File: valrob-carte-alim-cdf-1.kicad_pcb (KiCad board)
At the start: 4 copper layers, 87 x 57 mm, 201 parts, among them J1 USB_C_Receptacle_USB2.0_14P, J10 Conn_01x02, J11 Conn_01x02, J12 Conn_01x02, J13 Conn_01x02, J14 Conn_01x02, J15 Conn_01x02, J16 Conn_01x02, J17 Conn_01x02, J18 Conn_01x02, J19 Conn_01x02, J2 Conn_01x02, J20 Conn_01x02, J21 Conn_01x02, J22 Conn_01x02, J3 Conn_01x04_Pin, J4 Conn_01x02, J5 Conn_01x02, J6 Conn_01x02, J7 Conn_01x02, J8 Conn_01x02, J9 Conn_01x02, SW1 SW_Push, SW2 SW_Push, SW3 SW_Push, U1 SN65HVD230, U10 TPS259472A, U11 TPS259472A, U12 TPS259472A, U2 ESP32-S3-WROOM-1, U3 TLV75733PDBV, U4 TPS56A37, U5 TPS56A37, U6 TPS259472A, U7 TPS259472A, U8 TPS259472A, U9 TPS259472A

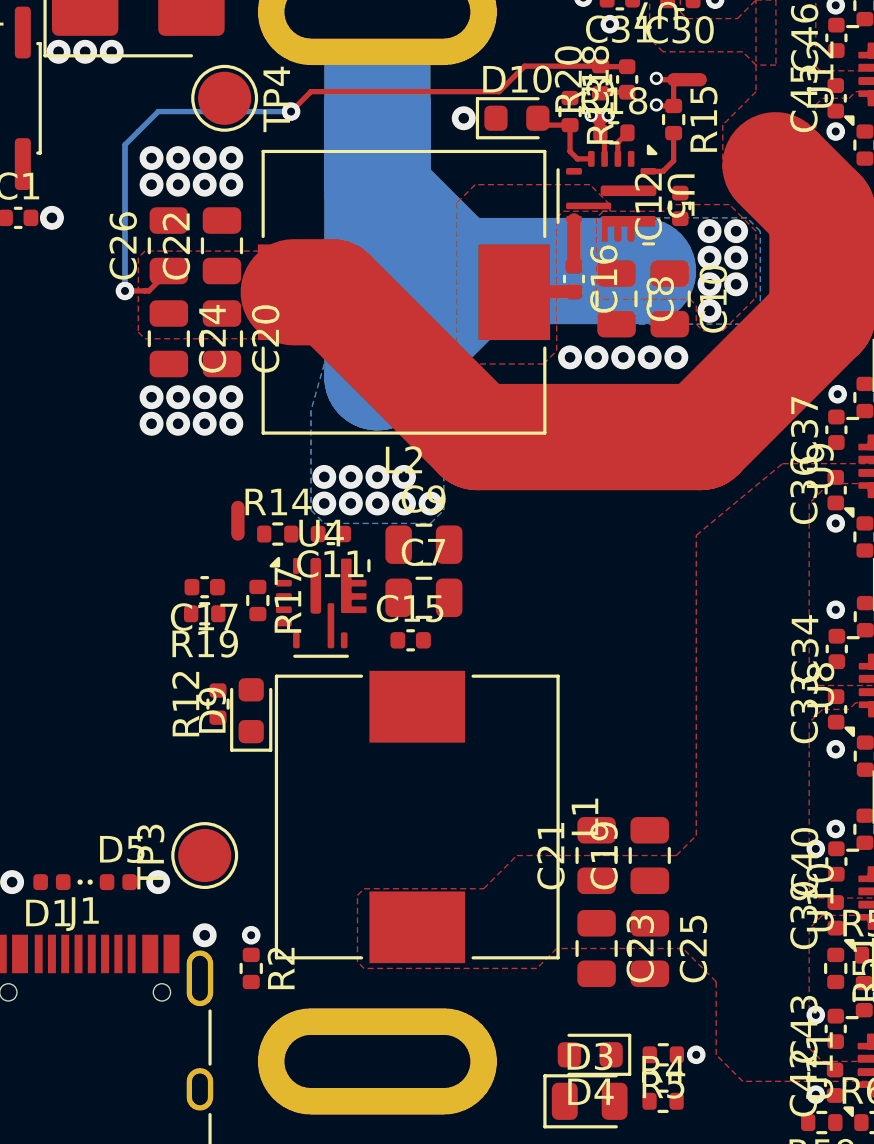
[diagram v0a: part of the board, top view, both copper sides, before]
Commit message: pcb: add 12V SMPS routing
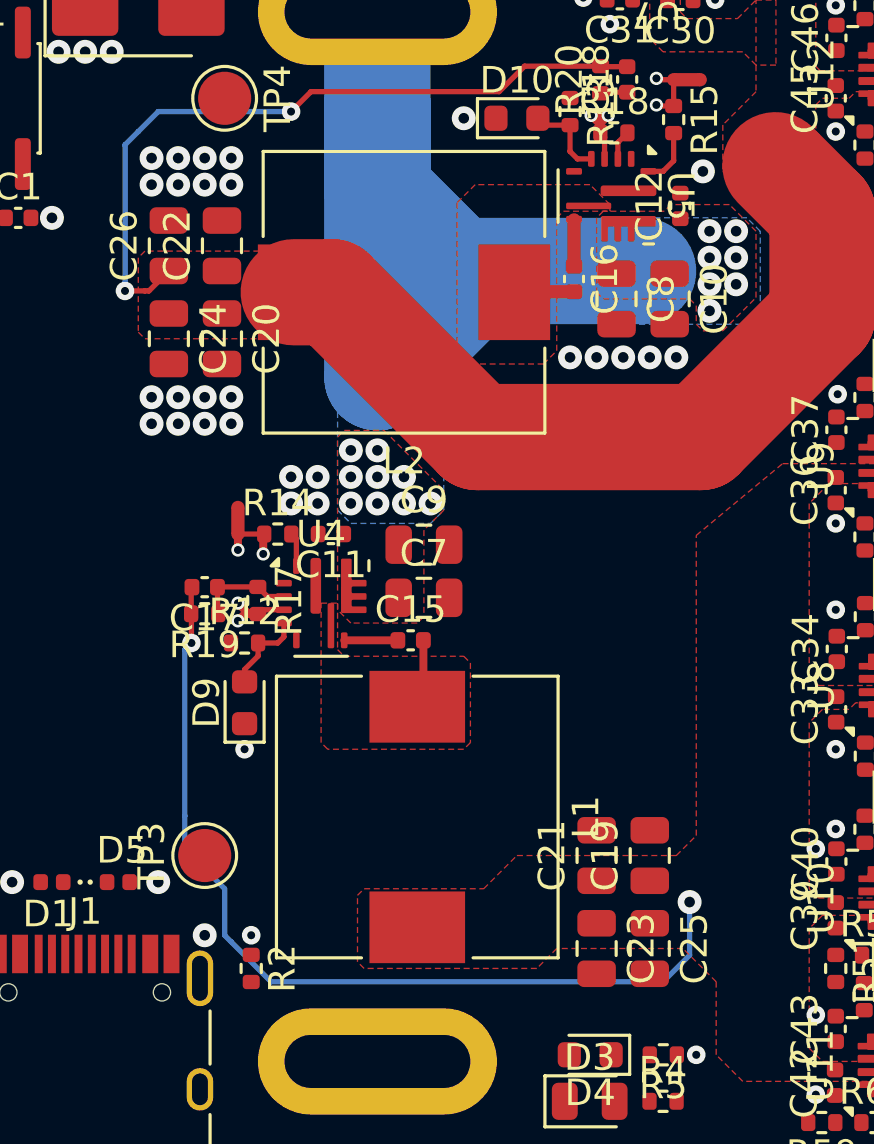
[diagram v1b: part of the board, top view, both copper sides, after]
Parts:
- moved R12 2.51 mm to (120.5, 90.2), turned to 0 degrees
- moved D9 0.39 mm to (120.5, 92.5)
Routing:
- net +12V: track 0.00 -> 34.5 mm, vias 0 -> 2
- net AGND: track 0.00 -> 5.18 mm, vias 0 -> 4
- net Net-(U4-FB): track 0.00 -> 3.67 mm
- net /PG_12V: track 0.00 -> 3.26 mm
- net Net-(U4-SW): track 0.00 -> 2.60 mm
- net Net-(U4-BOOT): track 0.00 -> 2.02 mm
- net Net-(U4-MODE): track 0.00 -> 1.28 mm
- net GND: vias 103 -> 109
- added copper zone on In1.Cu, net AGND
- added copper zone on F.Cu, net Net-(U4-SW)

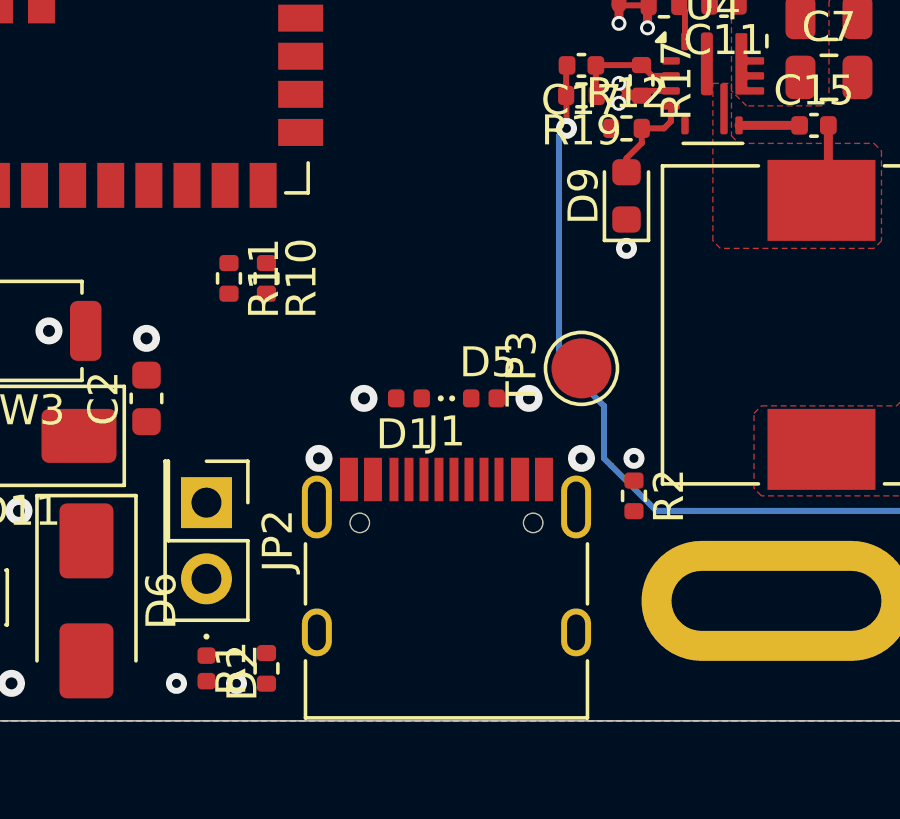
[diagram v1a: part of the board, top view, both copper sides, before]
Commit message: pcb: add usb routing
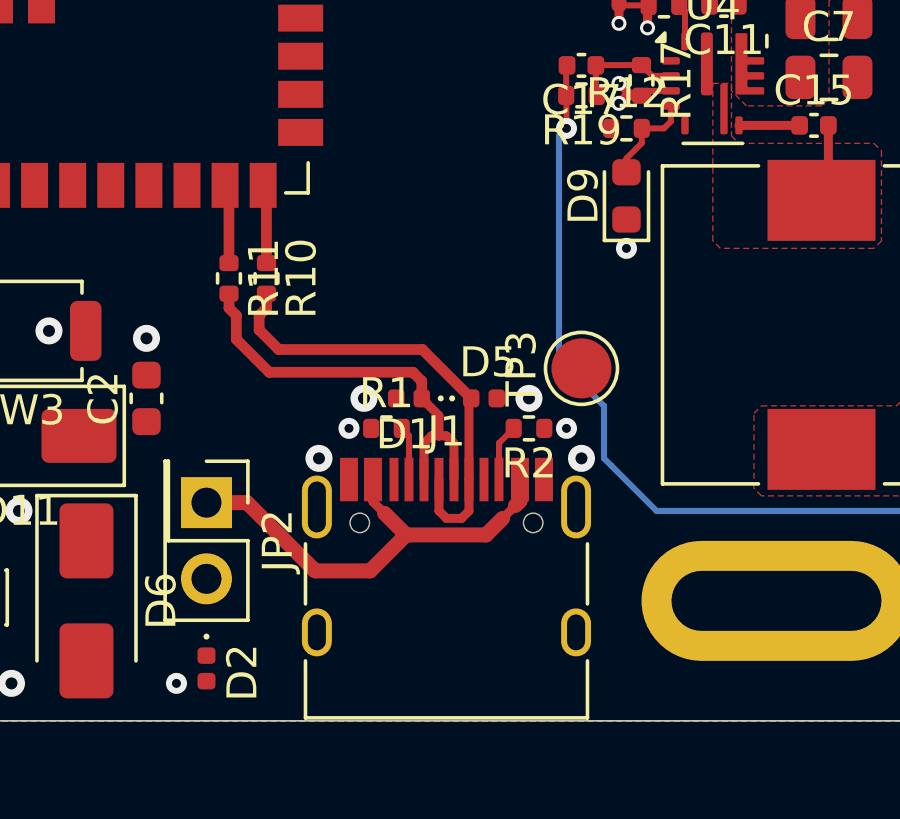
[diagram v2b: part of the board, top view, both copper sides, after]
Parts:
- moved R1 8.94 mm to (112.5, 100.2), turned to 0 degrees
- moved R2 4.16 mm to (117.2, 100.2), turned to 180 degrees
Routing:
- net VBUS: track 0.00 -> 15.4 mm
- net /D+: track 0.00 -> 15.4 mm
- net /D-: track 0.00 -> 14.1 mm
- net /ESP_D-: track 0.00 -> 2.64 mm
- net /ESP_D+: track 0.00 -> 2.64 mm
- net Net-(J1-CC2): track 0.00 -> 1.91 mm
- net Net-(J1-CC1): track 0.00 -> 1.80 mm

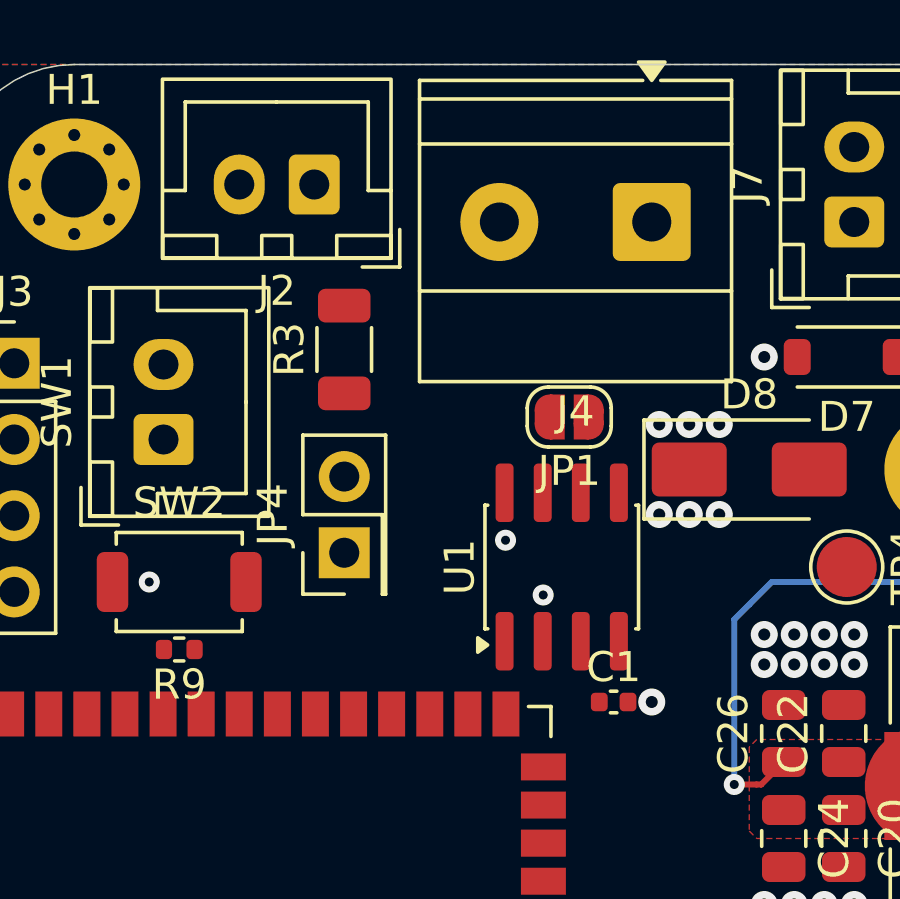
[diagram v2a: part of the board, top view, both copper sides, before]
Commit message: pcb: add can routing
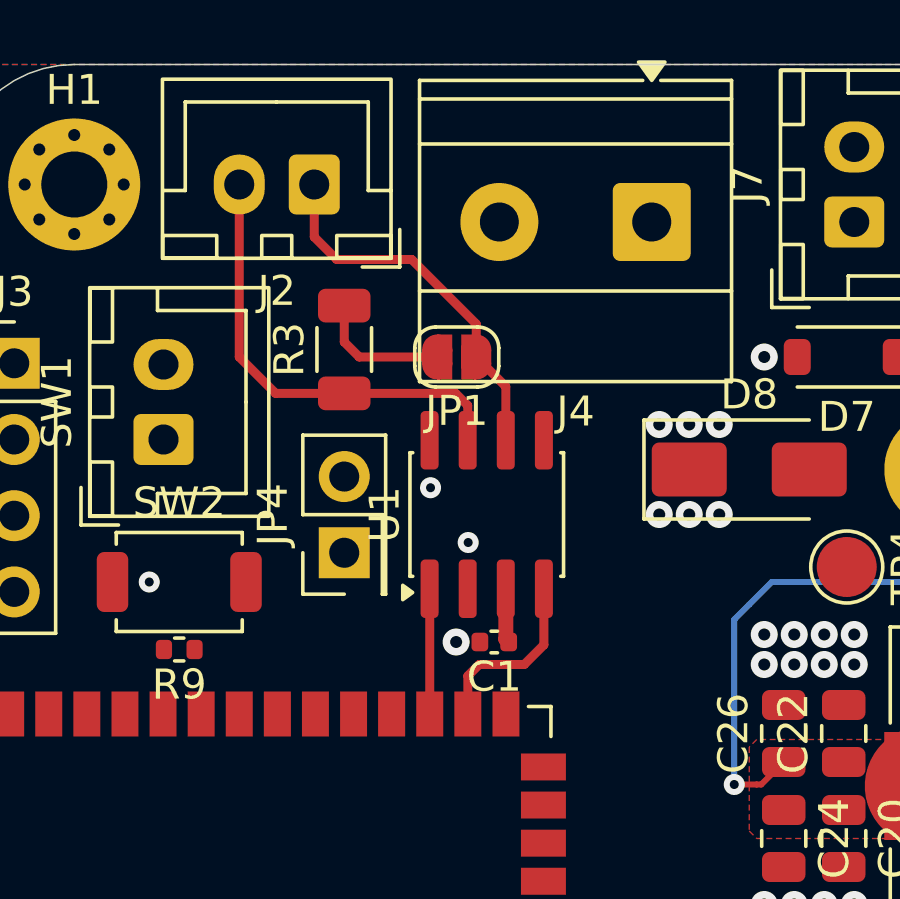
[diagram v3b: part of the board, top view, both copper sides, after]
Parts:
- moved C1 4.45 mm to (108.0, 72.2), turned to 180 degrees
- moved JP1 4.25 mm to (106.8, 62.8)
- moved U1 3.05 mm to (107.8, 68.0)
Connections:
- U2 pad 28: /BAU -> /CAN_RX
- U2 pad 29: /CAN_RX -> /CAN_TX
- U2 pad 30: /CAN_TX -> /BAU
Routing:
- net /CANH: track 0.00 -> 15.2 mm
- net /CANL: track 0.00 -> 12.6 mm
- net /CAN_RX: track 0.00 -> 6.10 mm
- net Net-(JP1-B): track 0.00 -> 4.52 mm
- net /CAN_TX: track 0.00 -> 4.18 mm
- net +3V3: track 0.00 -> 1.81 mm
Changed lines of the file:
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@@
 			(size 1.5 0.9)
 			(layers "F.Cu" "F.Mask" "F.Paste")
-			(net 89 "/BAU")
+			(net 91 "/CAN_RX")
 			(pinfunction "SPIIO6/GPIO35/FSPID/SUBSPID")
 			(pintype "bidirectional")
@@
 			(size 1.5 0.9)
 			(layers "F.Cu" "F.Mask" "F.Paste")
-			(net 91 "/CAN_RX")
+			(net 90 "/CAN_TX")
 			(pinfunction "SPIIO7/GPIO36/FSPICLK/SUBSPICLK")
 			(pintype "bidirectional")
@@
 			(size 1.5 0.9)
 			(layers "F.Cu" "F.Mask" "F.Paste")
-			(net 90 "/CAN_TX")
+			(net 89 "/BAU")
 			(pinfunction "SPIDQS/GPIO37/FSPIQ/SUBSPIQ")
 			(pintype "bidirectional")
@@
 	(footprint "Capacitor_SMD:C_0402_1005Metric"
 		(layer "F.Cu")
-		(at 111.98 74.25)
+		(at 108 72.25 180)
 		(descr "Capacitor SMD 0402 (1005 Metric), square (rectangular) end terminal, IPC-7351 nominal, (Body size source: IPC-SM-782 page 76, https://www.pcb-3d.com/wordpress/wp-content/uploads/ipc-sm-782a_amendment_1_and_2.pdf), generated with kicad-footprint-generator")
 		(tags "capacitor")
@@
 		)
 		(property "Basic" "Y"
-			(at 0 0 0)
+			(at 0 0 180)
 			(unlocked yes)
 			(layer "F.Fab")
@@
 		)
 		(property "JLCPCB Part #" "C307331"
-			(at 0 0 0)
+			(at 0 0 180)
 			(unlocked yes)
 			(layer "F.Fab")
@@
 		)
 		(property "Manufacturer" "Samsung Electro-Mechanics "
-			(at 0 0 0)
+			(at 0 0 180)
 			(unlocked yes)
 			(layer "F.Fab")
@@
 		)
 		(property "Manufacturer Part Number" "CL05B104KB54PNC"
-			(at 0 0 0)
+			(at 0 0 180)
 			(unlocked yes)
 			(layer "F.Fab")
@@
 		(attr smd)
 		(fp_line
-			(start -0.107836 -0.36)
-			(end 0.107836 -0.36)
+			(start -0.107836 0.36)
+			(end 0.107836 0.36)
 			(stroke
 				(width 0.12)
@@
 		)
 		(fp_line
-			(start -0.107836 0.36)
-			(end 0.107836 0.36)
+			(start -0.107836 -0.36)
+			(end 0.107836 -0.36)
 			(stroke
 				(width 0.12)
@@
 		)
 		(pad "1" smd roundrect
-			(at -0.48 0)
+			(at -0.48 0 180)
 			(size 0.56 0.62)
 			(layers "F.Cu" "F.Mask" "F.Paste")
@@
 		)
 		(pad "2" smd roundrect
-			(at 0.48 0)
+			(at 0.48 0 180)
 			(size 0.56 0.62)
 			(layers "F.Cu" "F.Mask" "F.Paste")
@@
 	(footprint "Jumper:SolderJumper-2_P1.3mm_Open_RoundedPad1.0x1.5mm"
 		(layer "F.Cu")
-		(at 110.5 64.75 180)
+		(at 106.75 62.75 180)
 		(descr "SMD Solder Jumper, 1x1.5mm, rounded Pads, 0.3mm gap, open")
 		(tags "solder jumper open")
@@
 	(footprint "Package_SO:SOIC-8_3.9x4.9mm_P1.27mm"
 		(layer "F.Cu")
-		(at 110.25 69.75 90)
+		(at 107.75 68 90)
 		(descr "SOIC, 8 Pin (JEDEC MS-012AA, https://www.analog.com/media/en/package-pcb-resources/package/pkg_pdf/soic_narrow-r/r_8.pdf), generated with kicad-footprint-generator ipc_gullwing_generator.py")
 		(tags "SOIC SO")
@@
 	)
 	(via
-		(at 113.25 74.25)
+		(at 106.73 72.25)
 		(size 0.9)
 		(drill 0.4)
@@
 	)
 	(via
-		(at 109.631054 70.683564)
+		(at 107.131054 68.933564)
 		(size 0.7)
 		(drill 0.3)
@@
 	)
 	(via
-		(at 108.376122 68.857719)
+		(at 105.876122 67.107719)
 		(size 0.7)
 		(drill 0.3)
@@
 	)
 	(segment
+		(start 108.385 72.155)
+		(end 108.48 72.25)
+		(width 0.5)
+		(layer "F.Cu")
+		(net 3)
+	)
+	(segment
+		(start 108.385 70.475)
+		(end 108.385 72.155)
+		(width 0.5)
+		(layer "F.Cu")
+		(net 3)
+	)
+	(segment
 		(start 130.08 69.5)
 		(end 123 69.5)
@@
 	)
 	(segment
+		(start 102 58.75)
+		(end 102 57)
+		(width 0.3)
+		(layer "F.Cu")
+		(net 47)
+	)
+	(segment
+		(start 102.75 59.5)
+		(end 102 58.75)
+		(width 0.3)
+		(layer "F.Cu")
+		(net 47)
+	)
+	(segment
+		(start 107.4 61.65)
+		(end 105.25 59.5)
+		(width 0.3)
+		(layer "F.Cu")
+		(net 47)
+	)
+	(segment
+		(start 105.25 59.5)
+		(end 102.75 59.5)
+		(width 0.3)
+		(layer "F.Cu")
+		(net 47)
+	)
+	(segment
+		(start 107.4 62.75)
+		(end 107.4 61.65)
+		(width 0.3)
+		(layer "F.Cu")
+		(net 47)
+	)
+	(segment
+		(start 108.385 63.735)
+		(end 107.4 62.75)
+		(width 0.3)
+		(layer "F.Cu")
+		(net 47)
+	)
+	(segment
+		(start 108.385 65.525)
+		(end 108.385 63.735)
+		(width 0.3)
+		(layer "F.Cu")
+		(net 47)
+	)
+	(segment
+		(start 99.5 62.75)
+		(end 99.5 57)
+		(width 0.3)
+		(layer "F.Cu")
+		(net 48)
+	)
+	(segment
+		(start 106.7125 63.9625)
+		(end 103 63.9625)
+		(width 0.3)
+		(layer "F.Cu")
+		(net 48)
+	)
+	(segment
+		(start 103 63.9625)
+		(end 100.7125 63.9625)
+		(width 0.3)
+		(layer "F.Cu")
+		(net 48)
+	)
+	(segment
+		(start 100.7125 63.9625)
+		(end 99.5 62.75)
+		(width 0.3)
+		(layer "F.Cu")
+		(net 48)
+	)
+	(segment
+		(start 107.115 65.525)
+		(end 107.115 64.365)
+		(width 0.3)
+		(layer "F.Cu")
+		(net 48)
+	)
+	(segment
+		(start 107.115 64.365)
+		(end 106.7125 63.9625)
+		(width 0.3)
+		(layer "F.Cu")
+		(net 48)
+	)
+	(segment
+		(start 103.5 62.75)
+		(end 103 62.25)
+		(width 0.3)
+		(layer "F.Cu")
+		(net 57)
+	)
+	(segment
+		(start 103 62.25)
+		(end 103 61.0375)
+		(width 0.3)
+		(layer "F.Cu")
+		(net 57)
+	)
+	(segment
+		(start 106.1 62.75)
+		(end 103.5 62.75)
+		(width 0.3)
+		(layer "F.Cu")
+		(net 57)
+	)
+	(segment
 		(start 121.16 89)
 		(end 121.98 89)
@@
 		(net 70)
 	)
+	(segment
+		(start 105.85 74.65)
+		(end 105.85 70.48)
+		(width 0.3)
+		(layer "F.Cu")
+		(net 90)
+	)
+	(segment
+		(start 105.85 70.48)
+		(end 105.845 70.475)
+		(width 0.3)
+		(layer "F.Cu")
+		(net 90)
+	)
+	(segment
+		(start 109 73)
+		(end 109.655 72.345)
+		(width 0.3)
+		(layer "F.Cu")
+		(net 91)
+	)
+	(segment
+		(start 107.12 74.65)
+		(end 107.12 73.38)
+		(width 0.3)
+		(layer "F.Cu")
+		(net 91)
+	)
+	(segment
+		(start 107.5 73)
+		(end 109 73)
+		(width 0.3)
+		(layer "F.Cu")
+		(net 91)
+	)
+	(segment
+		(start 109.655 72.345)
+		(end 109.655 70.475)
+		(width 0.3)
+		(layer "F.Cu")
+		(net 91)
+	)
+	(segment
+		(start 107.12 73.38)
+		(end 107.5 73)
+		(width 0.3)
+		(layer "F.Cu")
+		(net 91)
+	)
 	(zone
